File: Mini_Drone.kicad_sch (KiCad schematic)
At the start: 70 parts, among them J1 Conn_01x02, J3 Conn_01x02, J4 Conn_01x06, J7 Conn_01x11, J8 Conn_01x11, Q1 AO3400A, Q2 AO3400A, Q3 AO3400A, Q4 AO3400A, U1 ESP32-S3-WROOM-1, U2 MPU_6050_Module, U3 SPX3819M5-L-3-3

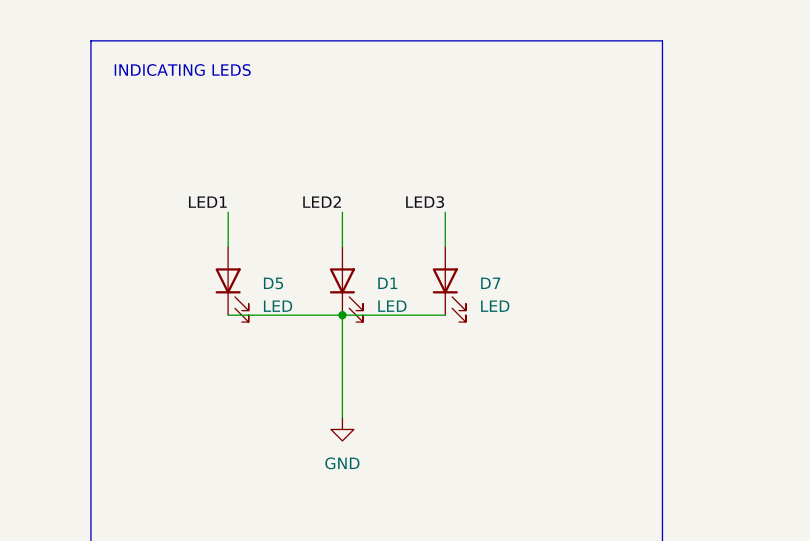
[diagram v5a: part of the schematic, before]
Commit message: need to add power indicating led and if possible add the switches
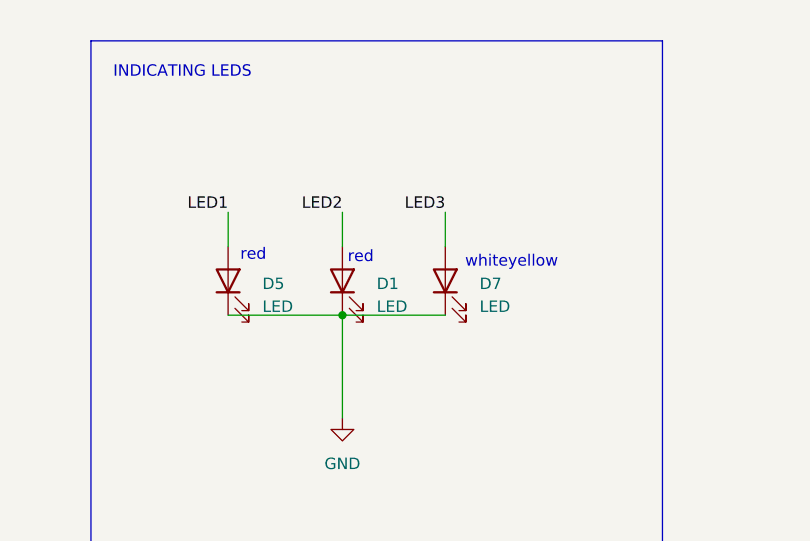
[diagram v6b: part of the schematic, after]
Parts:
- D1: LCSC Part # C22371297 -> C2286
- D5: LCSC Part # C965799 -> C2286
- D7: LCSC Part # C19171394 -> C2290
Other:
- note added: "red"
- note added: "whiteyellow"
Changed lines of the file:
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@@
 		)
 	)
+	(text "red "
+		(exclude_from_sim no)
+		(at 316.484 44.196 0)
+		(effects
+			(font
+				(size 1.27 1.27)
+			)
+		)
+	)
+	(text "red "
+		(exclude_from_sim no)
+		(at 328.422 44.45 0)
+		(effects
+			(font
+				(size 1.27 1.27)
+			)
+		)
+	)
 	(text "INDICATING LEDS\n\n\n\n"
 		(exclude_from_sim no)
@@
 		)
 	)
+	(text "whiteyellow\n"
+		(exclude_from_sim no)
+		(at 345.186 44.958 0)
+		(effects
+			(font
+				(size 1.27 1.27)
+			)
+		)
+	)
 	(text "Voltage_Regulator\n"
 		(exclude_from_sim no)
@@
 			)
 		)
-		(property "LCSC Part #" "C965799"
+		(property "LCSC Part #" "C2286"
 			(at 313.69 46.99 90)
 			(effects
@@
 			)
 		)
-		(property "LCSC Part #" "C22371297"
+		(property "LCSC Part #" "C2286"
 			(at 326.39 46.99 90)
 			(effects
@@
 			)
 		)
-		(property "LCSC Part #" "C19171394"
+		(property "LCSC Part #" "C2290"
 			(at 337.82 46.99 90)
 			(effects

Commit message: Hari version switchled
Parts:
- added D8, D9: LED, LED_SMD:LED_0603_1608Metric, symbol Device:LED
- added R10: 220, Resistor_SMD:R_0603_1608Metric, symbol Mini_Drone_prj:R
- added R11: 220, Resistor_SMD:R_0603_1608Metric, symbol Device:R
- added S2: 500SSP1S1M2REA, Mini_Drone_prj:SW_500SSP1S1M2REA, symbol Mini_Drone_prj:500SSP1S1M2REA
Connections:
- net +3V3: now also R11.2
- net BAT+: now also R10.2, S2.2; no longer U3.3 (EN)
- net GND: now also D8.1 (K), D9.1 (K)
- new net: S2.1, U3.3 (EN)
- new net: D8.2 (A), R10.1
- new net: D9.2 (A), R11.1
- no-connect marks 4 -> 5

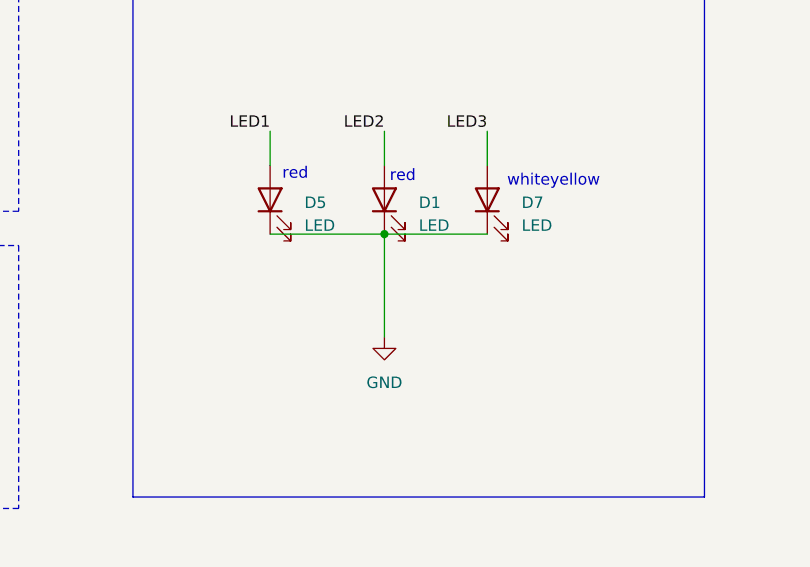
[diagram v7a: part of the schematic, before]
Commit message: needs to increase the outline
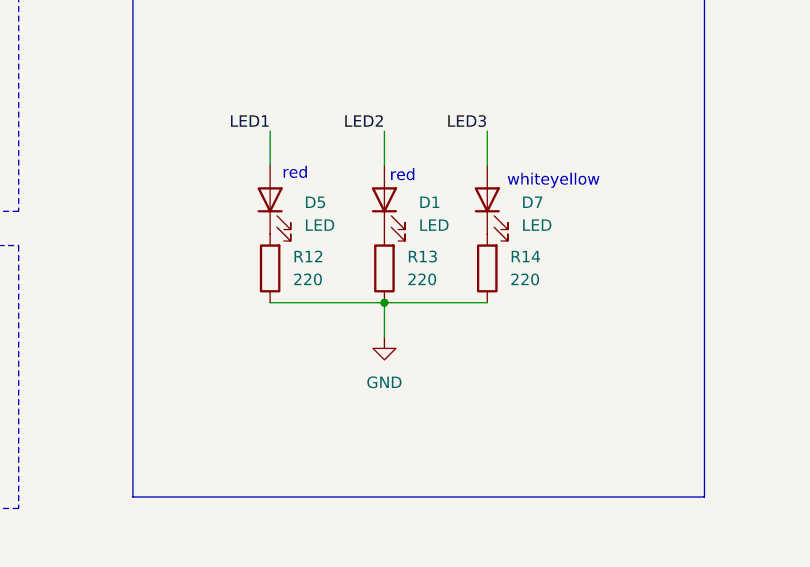
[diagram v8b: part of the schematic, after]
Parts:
- added R12, R13, R14: 220, Resistor_SMD:R_0201_0603Metric, symbol Mini_Drone_prj:R
- R10: footprint Resistor_SMD:R_0603_1608Metric -> Resistor_SMD:R_0201_0603Metric
- S2: footprint Mini_Drone_prj:SW_500SSP1S1M2REA -> 500SSP1S1M2REA:SW_500SSP1S1M2REA; LCSC Part # (none) -> C92655
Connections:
- net GND: now also R12.1, R13.1, R14.1; no longer D1.1 (K), D5.1 (K), D7.1 (K)
- new net: D5.1 (K), R12.2
- new net: D1.1 (K), R13.2
- new net: D7.1 (K), R14.2
